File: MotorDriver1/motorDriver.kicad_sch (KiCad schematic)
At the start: 23 parts, among them Q1 IRLZ44N, Q2 IRLZ44N, Q3 IRLZ44N, Q4 IRLZ44N

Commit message: laid out PCB
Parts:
- Conn1: renamed from Motor1+1; value Motor1- -> Motor1; footprint (none) -> Connector_PinHeader_2.54mm:PinHeader_1x02_P2.54mm_Vertical
- Conn2: renamed from Motor2+1; value Motor2- -> Motor2; footprint (none) -> Connector_PinHeader_2.54mm:PinHeader_1x02_P2.54mm_Vertical
- Conn3: renamed from Motor1+2; value Motor1- -> Motor3; footprint (none) -> Connector_PinHeader_2.54mm:PinHeader_1x02_P2.54mm_Vertical
- Conn4: renamed from Motor2+2; value Motor2- -> Motor4; footprint (none) -> Connector_PinHeader_2.54mm:PinHeader_1x02_P2.54mm_Vertical
- R1, R2, R3, R4, R5, R6, R7, R8: footprint (none) -> Resistor_SMD:R_0402_1005Metric
- VBAT1: footprint (none) -> Connector_PinHeader_2.54mm:PinHeader_1x02_P2.54mm_Vertical
- renumbered D3 to D2, D2 to D3, Q3 to Q2, Q2 to Q3
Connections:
- net Motor1Sig renamed Motor1_PWM
- net Motor2Sig renamed Motor2_PWM
- net Motor3Sig renamed Motor3_PWM
- net Motor4Sig renamed Motor4_PWM
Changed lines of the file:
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@@
 		)
 	)
-	(global_label "Motor3Sig"
+	(global_label "Motor3_PWM"
 		(shape input)
 		(at 68.58 144.78 180)
@@
 		)
 		(property "Intersheetrefs" "${INTERSHEET_REFS}"
-			(at 56.1607 144.78 0)
+			(at 53.9836 144.78 0)
 			(effects
 				(font
@@
 		)
 	)
-	(global_label "Motor2Sig"
+	(global_label "Motor2_PWM"
 		(shape input)
 		(at 106.68 62.23 180)
@@
 		)
 		(property "Intersheetrefs" "${INTERSHEET_REFS}"
-			(at 94.2607 62.23 0)
+			(at 92.0836 62.23 0)
 			(effects
 				(font
@@
 		)
 	)
-	(global_label "Motor1Sig"
+	(global_label "Motor1_PWM"
 		(shape input)
 		(at 62.23 62.23 180)
@@
 		)
 		(property "Intersheetrefs" "${INTERSHEET_REFS}"
-			(at 49.8107 62.23 0)
+			(at 47.6336 62.23 0)
 			(effects
 				(font
@@
 		)
 	)
-	(global_label "Motor4Sig"
+	(global_label "Motor4_PWM"
 		(shape input)
 		(at 113.03 144.78 180)
@@
 		)
 		(property "Intersheetrefs" "${INTERSHEET_REFS}"
-			(at 100.6107 144.78 0)
+			(at 98.4336 144.78 0)
 			(effects
 				(font
@@
 			)
 		)
-		(property "Footprint" ""
+		(property "Footprint" "Resistor_SMD:R_0402_1005Metric"
 			(at 65.532 69.85 90)
 			(effects
@@
 			)
 		)
-		(property "Footprint" ""
+		(property "Footprint" "Resistor_SMD:R_0402_1005Metric"
 			(at 78.232 77.47 90)
 			(effects
@@
 			)
 		)
-		(property "Footprint" ""
+		(property "Footprint" "Resistor_SMD:R_0402_1005Metric"
 			(at 71.882 152.4 90)
 			(effects
@@
 		(dnp no)
 		(fields_autoplaced yes)
-		(property "Reference" "Q2"
+		(property "Reference" "Q3"
 			(at 90.17 143.5099 0)
 			(effects
@@
 			(project "MotorDriver1"
 				(path "/79cc9cfe-04d6-4d00-aa84-feae66cf8c45/bb18fbb4-ec68-4ac2-b714-52f61fe72a01"
-					(reference "Q2")
+					(reference "Q3")
 					(unit 1)
 				)
@@
 		(on_board yes)
 		(dnp no)
-		(property "Reference" "Motor1+2"
+		(property "Reference" "Conn3"
 			(at 60.96 116.8399 0)
 			(effects
@@
 			)
 		)
-		(property "Value" "Motor1-"
+		(property "Value" "Motor3"
 			(at 61.468 119.634 0)
 			(effects
@@
 			)
 		)
-		(property "Footprint" ""
+		(property "Footprint" "Connector_PinHeader_2.54mm:PinHeader_1x02_P2.54mm_Vertical"
 			(at 58.42 116.84 0)
 			(effects
@@
 			(project "MotorDriver1"
 				(path "/79cc9cfe-04d6-4d00-aa84-feae66cf8c45/bb18fbb4-ec68-4ac2-b714-52f61fe72a01"
-					(reference "Motor1+2")
+					(reference "Conn3")
 					(unit 1)
 				)
@@
 		(dnp no)
 		(fields_autoplaced yes)
-		(property "Reference" "Motor2+2"
+		(property "Reference" "Conn4"
 			(at 60.96 125.7299 0)
 			(effects
@@
 			)
 		)
-		(property "Value" "Motor2-"
+		(property "Value" "Motor4"
 			(at 60.96 128.2699 0)
 			(effects
@@
 			)
 		)
-		(property "Footprint" ""
+		(property "Footprint" "Connector_PinHeader_2.54mm:PinHeader_1x02_P2.54mm_Vertical"
 			(at 58.42 125.73 0)
 			(effects
@@
 			(project "MotorDriver1"
 				(path "/79cc9cfe-04d6-4d00-aa84-feae66cf8c45/bb18fbb4-ec68-4ac2-b714-52f61fe72a01"
-					(reference "Motor2+2")
+					(reference "Conn4")
 					(unit 1)
 				)
@@
 		(dnp no)
 		(fields_autoplaced yes)
-		(property "Reference" "Motor2+1"
+		(property "Reference" "Conn2"
 			(at 54.61 43.1799 0)
 			(effects
@@
 			)
 		)
-		(property "Value" "Motor2-"
+		(property "Value" "Motor2"
 			(at 54.61 45.7199 0)
 			(effects
@@
 			)
 		)
-		(property "Footprint" ""
+		(property "Footprint" "Connector_PinHeader_2.54mm:PinHeader_1x02_P2.54mm_Vertical"
 			(at 52.07 43.18 0)
 			(effects
@@
 			(project "MotorDriver1"
 				(path "/79cc9cfe-04d6-4d00-aa84-feae66cf8c45/bb18fbb4-ec68-4ac2-b714-52f61fe72a01"
-					(reference "Motor2+1")
+					(reference "Conn2")
 					(unit 1)
 				)
@@
 			)
 		)
-		(property "Footprint" ""
+		(property "Footprint" "Resistor_SMD:R_0402_1005Metric"
 			(at 115.062 152.4 90)
 			(effects
@@
 			)
 		)
-		(property "Footprint" ""
+		(property "Footprint" "Connector_PinHeader_2.54mm:PinHeader_1x02_P2.54mm_Vertical"
 			(at 229.87 50.8 0)
 			(effects
@@
 		(on_board yes)
 		(dnp no)
-		(property "Reference" "Motor1+1"
+		(property "Reference" "Conn1"
 			(at 54.61 34.2899 0)
 			(effects
@@
 			)
 		)
-		(property "Value" "Motor1-"
+		(property "Value" "Motor1"
 			(at 55.118 37.084 0)
 			(effects
@@
 			)
 		)
-		(property "Footprint" ""
+		(property "Footprint" "Connector_PinHeader_2.54mm:PinHeader_1x02_P2.54mm_Vertical"
 			(at 52.07 34.29 0)
 			(effects
@@
 			(project "MotorDriver1"
 				(path "/79cc9cfe-04d6-4d00-aa84-feae66cf8c45/bb18fbb4-ec68-4ac2-b714-52f61fe72a01"
-					(reference "Motor1+1")
+					(reference "Conn1")
 					(unit 1)
 				)
@@
 		(dnp no)
 		(fields_autoplaced yes)
-		(property "Reference" "Q3"
+		(property "Reference" "Q2"
 			(at 127 60.9599 0)
 			(effects
@@
 			(project "MotorDriver1"
 				(path "/79cc9cfe-04d6-4d00-aa84-feae66cf8c45/bb18fbb4-ec68-4ac2-b714-52f61fe72a01"
-					(reference "Q3")
+					(reference "Q2")
 					(unit 1)
 				)
@@
 			)
 		)
-		(property "Footprint" ""
+		(property "Footprint" "Resistor_SMD:R_0402_1005Metric"
 			(at 84.582 160.02 90)
 			(effects
@@
 			)
 		)
-		(property "Footprint" ""
+		(property "Footprint" "Resistor_SMD:R_0402_1005Metric"
 			(at 108.712 69.85 90)
 			(effects
@@
 			)
 		)
-		(property "Footprint" ""
+		(property "Footprint" "Resistor_SMD:R_0402_1005Metric"
 			(at 127.762 160.02 90)
 			(effects
@@
 		(dnp no)
 		(fields_autoplaced yes)
-		(property "Reference" "D3"
+		(property "Reference" "D2"
 			(at 115.57 50.7999 90)
 			(effects
@@
 			(project "MotorDriver1"
 				(path "/79cc9cfe-04d6-4d00-aa84-feae66cf8c45/bb18fbb4-ec68-4ac2-b714-52f61fe72a01"
-					(reference "D3")
+					(reference "D2")
 					(unit 1)
 				)
@@
 			)
 		)
-		(property "Footprint" ""
+		(property "Footprint" "Resistor_SMD:R_0402_1005Metric"
 			(at 121.412 77.47 90)
 			(effects
@@
 		(dnp no)
 		(fields_autoplaced yes)
-		(property "Reference" "D2"
+		(property "Reference" "D3"
 			(at 78.74 133.3499 90)
 			(effects
@@
 			(project "MotorDriver1"
 				(path "/79cc9cfe-04d6-4d00-aa84-feae66cf8c45/bb18fbb4-ec68-4ac2-b714-52f61fe72a01"
-					(reference "D2")
-					(unit 1)
-				)
+					(reference "D3")
+					(unit 1)
+				)

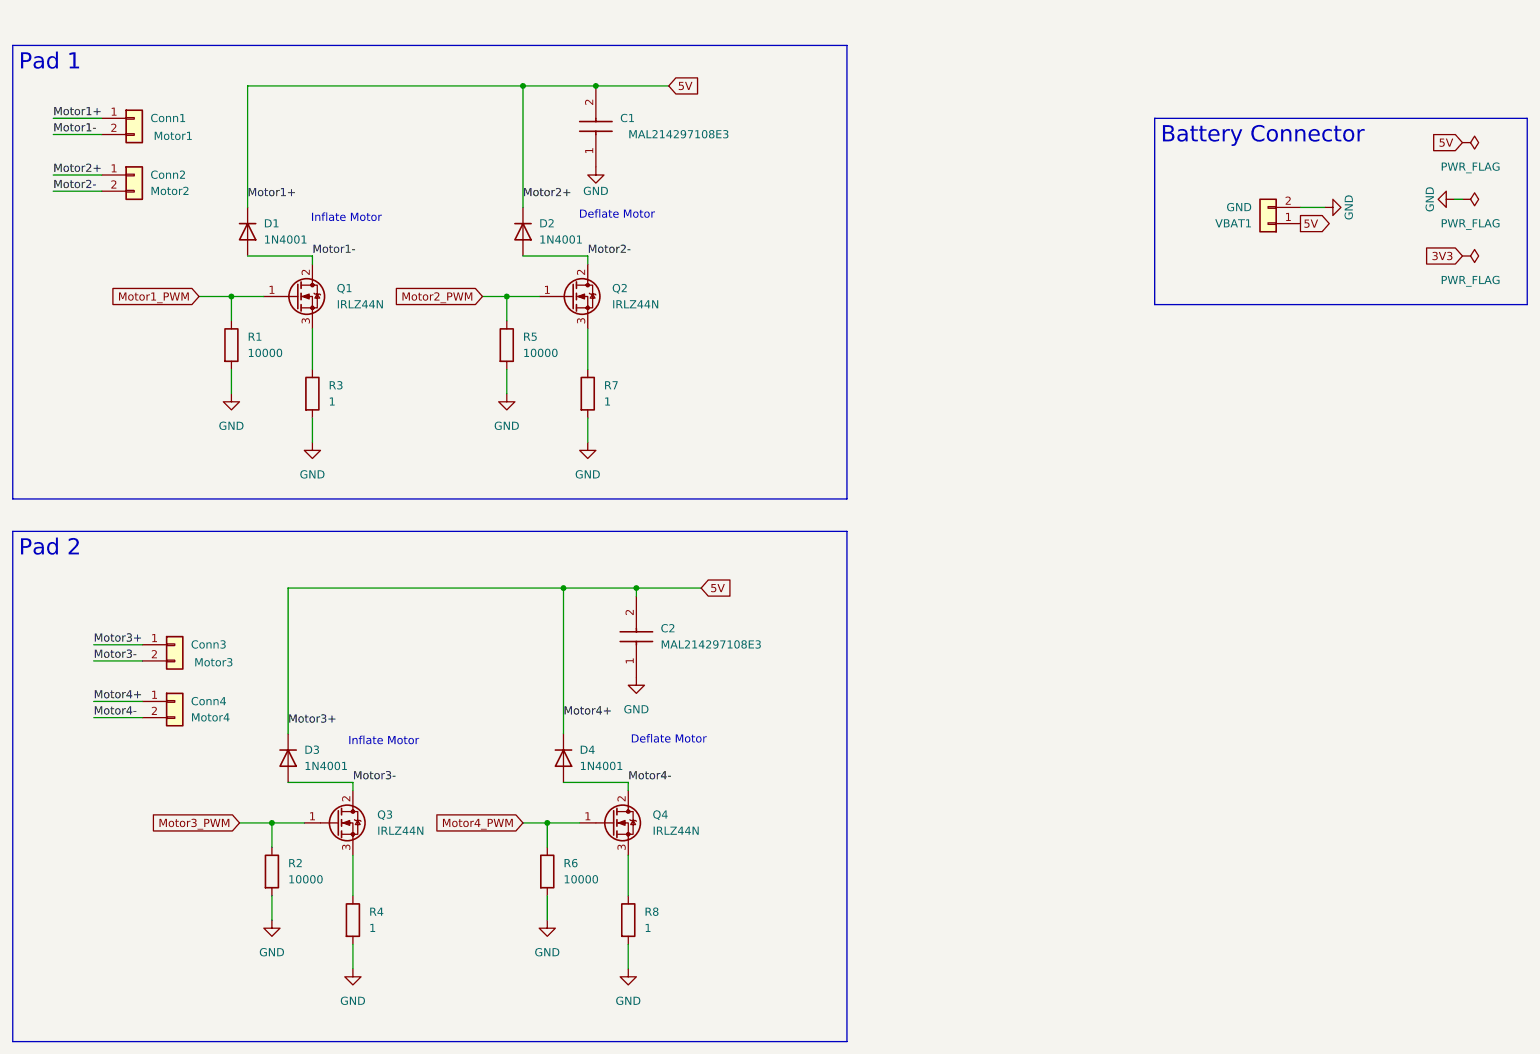
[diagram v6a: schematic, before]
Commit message: component placing and first traces
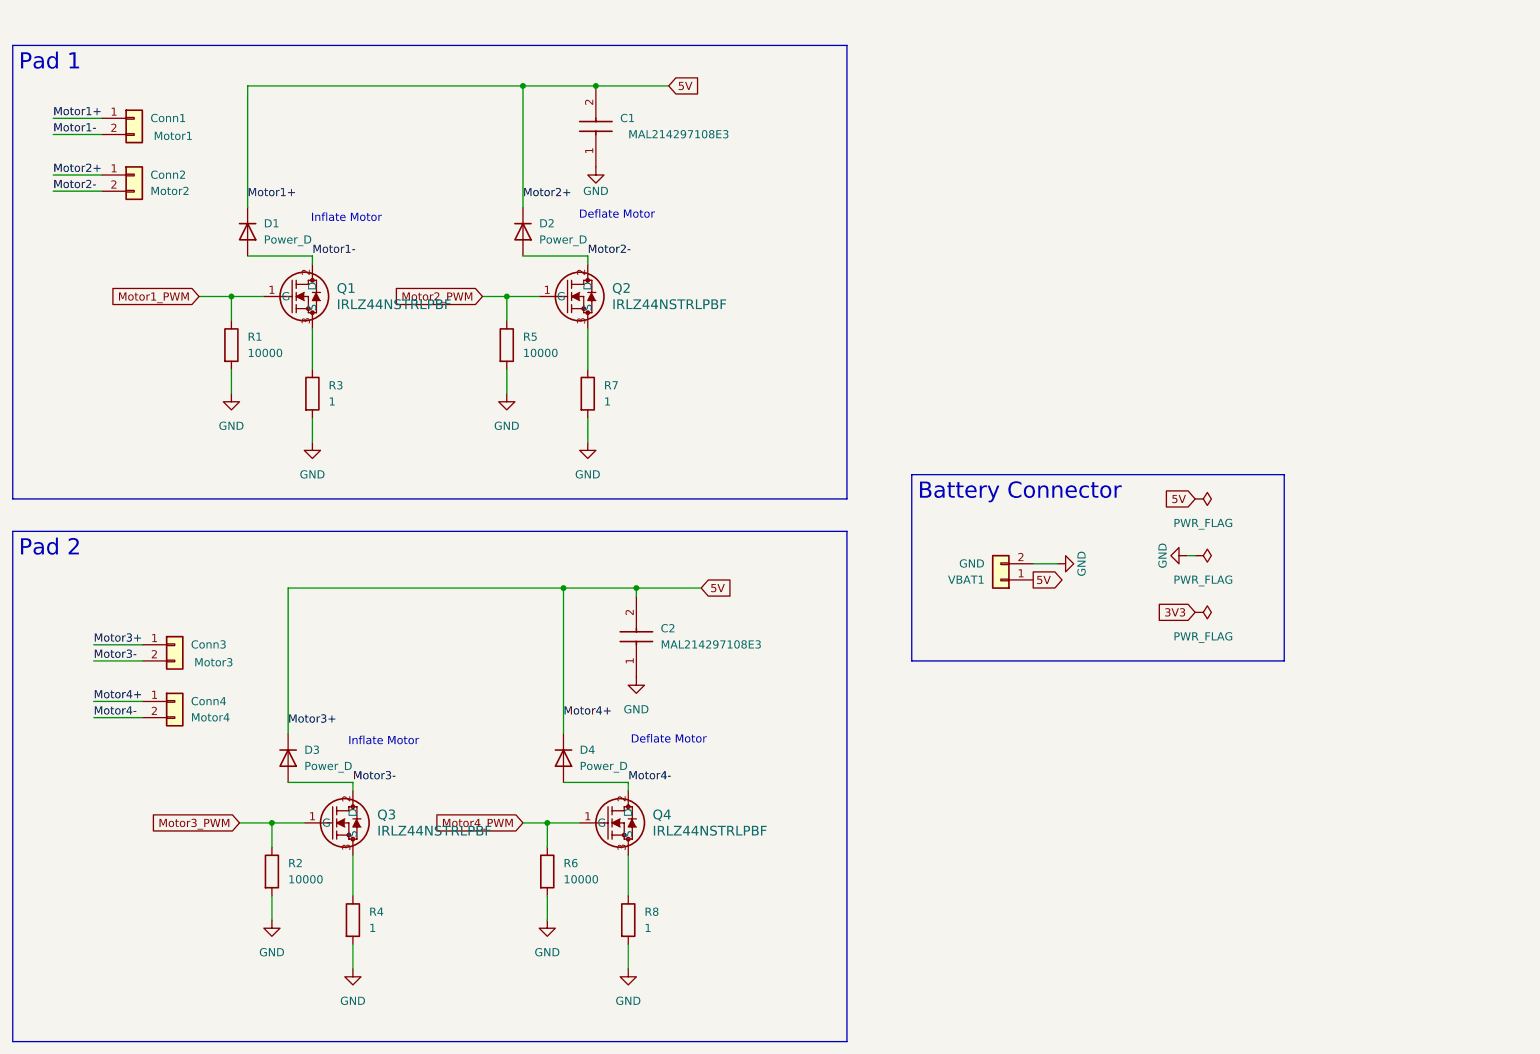
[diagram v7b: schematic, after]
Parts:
- removed Q1, Q2, Q3, Q4: IRLZ44N, Package_TO_SOT_THT:TO-220-3_Vertical, symbol Transistor_FET:IRLZ44N
- added Q1, Q2, Q3, Q4: IRLZ44NSTRLPBF, NMOSGDS_D2PAK_INF, symbol pcb:IRLZ44NSTRLPBF
- D1, D2, D3, D4: value 1N4001 -> Power_D; footprint Diode_THT:D_DO-41_SOD81_P10.16mm_Horizontal -> Diode_SMD:D_0201_0603Metric
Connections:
- net Motor1-: now also Q1.2 (D)
- net Motor1_PWM: now also Q1.1 (G)
- net Motor2-: now also Q2.2 (D)
- net Motor2_PWM: now also Q2.1 (G)
- net Motor3-: now also Q3.2 (D)
- net Motor3_PWM: now also Q3.1 (G)
- net Motor4-: now also Q4.2 (D)
- net Motor4_PWM: now also Q4.1 (G)
- net at R8.1: now also Q4.3 (S)
- net at R3.1: now also Q1.3 (S)
- net at R4.1: now also Q3.3 (S)
- net at R7.1: now also Q2.3 (S)
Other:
- moved on the sheet: VBAT1

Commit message: Updated crystal footprints
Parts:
- Q1, Q2, Q3, Q4: footprint NMOSGDS_D2PAK_INF -> footprintLib:NMOSGDS_D2PAK_INF
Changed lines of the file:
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@@
 			)
 		)
-		(property "Footprint" "NMOSGDS_D2PAK_INF"
+		(property "Footprint" "footprintLib:NMOSGDS_D2PAK_INF"
 			(at 115.57 62.23 0)
 			(effects
@@
 			)
 		)
-		(property "Footprint" "NMOSGDS_D2PAK_INF"
+		(property "Footprint" "footprintLib:NMOSGDS_D2PAK_INF"
 			(at 72.39 62.23 0)
 			(effects
@@
 			)
 		)
-		(property "Footprint" "NMOSGDS_D2PAK_INF"
+		(property "Footprint" "footprintLib:NMOSGDS_D2PAK_INF"
 			(at 121.92 144.78 0)
 			(effects
@@
 			)
 		)
-		(property "Footprint" "NMOSGDS_D2PAK_INF"
+		(property "Footprint" "footprintLib:NMOSGDS_D2PAK_INF"
 			(at 78.74 144.78 0)
 			(effects
